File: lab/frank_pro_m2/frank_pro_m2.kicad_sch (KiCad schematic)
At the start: 12 parts, among them J1 UART, J2 PWR

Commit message: LAB WIP
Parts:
- removed JP1: Config Switches, FRANK:SOIC127P830X260-12N, symbol Switch:SW_DIP_x06
- added J3: PWR, FRANK:Pin Header (1x03), symbol Connector:Conn_01x03_Pin
- added JP1: Config Switches, FRANK:DS05127204BKSMTTR, symbol DS05-127-2-04BK-SMT-TR:DS05-127-2-04BK-SMT-TR
- added S1: MSK12C02, FRANK:SW_MSK12C02, symbol MSK12C02:MSK12C02
- added S3: RP BOOT, FRANK:TS-1234VW, symbol FRANK:SW_Push_1234VW
- added S4: RP Reset, FRANK:KMR_2, symbol KMR221G_LFS:KMR221G_LFS
- added S5: RP BOOT, FRANK:KMR_2, symbol KMR221G_LFS:KMR221G_LFS
- added S6: ESP Reset, FRANK:TS-1234VW, symbol FRANK:SW_Push_1234VW
- J1: footprint FRANK:Pin Header (1x03) -> FRANK:JST_SH_BM04B-SRSS-TB_1x04-1MP_P1.00mm_Vertical; symbol Connector:Conn_01x03_Pin -> Connector:Conn_01x04_Pin
- J2: value PWR -> DEBUG; footprint FRANK:Pin Header (1x03) -> FRANK:JST_SH_BM03B-SRSS-TB_1x03-1MP_P1.00mm_Vertical
- S2: renamed from S1; value Reset -> RP Reset; footprint FRANK:TACT-SIDE-4623 -> FRANK:TS-1234VW; symbol Switch:SW_Push -> FRANK:SW_Push_1234VW
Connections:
- net +3V3: now also J1.2 (Pin_2), J3.1 (Pin_1), JP1.4 (NO_2); no longer J2.1 (Pin_1)
- net AMP_L: now also JP1.7 (COM_4)
- net AUDIOSW: now also JP1.1 (COM_1)
- net ESP_RST: now also S6.1
- net GND: now also J1.1 (Pin_1), S2.3 (GND), J3.2 (Pin_2), JP1.6 (NO_3), S1.4_1 (GND), S1.4_2 (GND), S1.4_3 (GND), S1.4_4 (GND), S3.2, S3.3 (GND), S4.2, S4.4, S5.2, S5.4, S6.2, S6.3 (GND); no longer J1.3 (Pin_3)
- net MONO_R: now also JP1.8 (NO_4)
- net MSPUP3V3: now also JP1.3 (COM_2)
- net PGPIO0: now also J1.3 (Pin_3); no longer J1.1 (Pin_1)
- net PGPIO1: now also J1.4 (Pin_4); no longer J1.2 (Pin_2)
- net PRUN: now also S4.1, S4.3
- net PSWCLK: now also J2.1 (Pin_1)
- net PSWDIO: now also J2.3 (Pin_3)
- net SHND: now also JP1.5 (COM_3)
- net UM_SW: now also S1.3
- net VBUS: now also J3.3 (Pin_3), JP1.2 (NO_1), S1.2; no longer J2.3 (Pin_3)
- new net PBOOTSEL: S3.1, S5.1, S5.3
- no-connect marks 32 -> 33
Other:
- moved on the sheet: J2

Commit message: Board updates
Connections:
- net AMP_L: no longer JP1.7 (COM_4)
- new net MONO_L: JP1.7 (COM_4)
- no-connect marks 33 -> 32

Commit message: Rename footprints, 3D models to KiCad standard naming
lab/xt8086:
- Renamed 22 footprints (spaces/parens/IPNs -> KiCad style)
- Renamed 13 3D models, normalized all to .step
- Fixed FRANK: prefix -> xt8086: in symbol/schematic refs
- Fixed bare 3D model path without ${KIPRJMOD} prefix

lab/frank_pro_m2:
- Removed 11 unused footprints
- Renamed 32 footprints to KiCad standard naming
- Renamed 33 3D models, normalized all to .step
- Fixed wrong library prefixes (LIBS:, DC-005-5A-2.0:, MSK12C02:, etc.)
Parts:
- H1, H2, H3, H4: footprint FRANK:Mounting Hole (2.7mm) -> FRANK:MountingHole_2.7mm
- J1: footprint FRANK:JST_SH_BM04B-SRSS-TB_1x04-1MP_P1.00mm_Vertical -> FRANK:JST_SH_1x04_P1.00mm_Vertical
- J2: footprint FRANK:JST_SH_BM03B-SRSS-TB_1x03-1MP_P1.00mm_Vertical -> FRANK:JST_SH_1x03_P1.00mm_Vertical
- J3: footprint FRANK:Pin Header (1x03) -> FRANK:PinHeader_1x03_P2.54mm
- JP1: footprint FRANK:DS05127204BKSMTTR -> FRANK:DIPSwitch_4pos_DS05
- S1: footprint FRANK:SW_MSK12C02 -> FRANK:Switch_Slide_MSK12C02
- S2, S3, S6: footprint FRANK:TS-1234VW -> FRANK:Button_SMD_TS1234VW
- S4, S5: footprint FRANK:KMR_2 -> FRANK:Button_SMD_3x4x2mm
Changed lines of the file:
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@@
 			)
 		)
-		(property "Footprint" "FRANK:SW_MSK12C02"
+		(property "Footprint" "FRANK:Switch_Slide_MSK12C02"
 			(at 173.99 95.25 0)
 			(hide yes)
@@
 			)
 		)
-		(property "Footprint" "FRANK:DS05127204BKSMTTR"
+		(property "Footprint" "FRANK:DIPSwitch_4pos_DS05"
 			(at 207.01 125.4 0)
 			(hide yes)
@@
 			)
 		)
-		(property "Footprint" "FRANK:KMR_2"
+		(property "Footprint" "FRANK:Button_SMD_3x4x2mm"
 			(at 234.95 166.04 0)
 			(hide yes)
@@
 			)
 		)
-		(property "Footprint" "FRANK:JST_SH_BM03B-SRSS-TB_1x03-1MP_P1.00mm_Vertical"
+		(property "Footprint" "FRANK:JST_SH_1x03_P1.00mm_Vertical"
 			(at 226.06 93.98 0)
 			(hide yes)
@@
 			)
 		)
-		(property "Footprint" "FRANK:Pin Header (1x03)"
+		(property "Footprint" "FRANK:PinHeader_1x03_P2.54mm"
 			(at 252.73 93.98 0)
 			(hide yes)
@@
 			)
 		)
-		(property "Footprint" "FRANK:TS-1234VW"
+		(property "Footprint" "FRANK:Button_SMD_TS1234VW"
 			(at 184.15 53.34 0)
 			(hide yes)
@@
 			)
 		)
-		(property "Footprint" "FRANK:TS-1234VW"
+		(property "Footprint" "FRANK:Button_SMD_TS1234VW"
 			(at 184.15 68.58 0)
 			(hide yes)
@@
 			)
 		)
-		(property "Footprint" "FRANK:JST_SH_BM04B-SRSS-TB_1x04-1MP_P1.00mm_Vertical"
+		(property "Footprint" "FRANK:JST_SH_1x04_P1.00mm_Vertical"
 			(at 204.47 93.98 0)
 			(hide yes)
@@
 			)
 		)
-		(property "Footprint" "FRANK:Mounting Hole (2.7mm)"
+		(property "Footprint" "FRANK:MountingHole_2.7mm"
 			(at 160.02 187.96 0)
 			(hide yes)
@@
 			)
 		)
-		(property "Footprint" "FRANK:Mounting Hole (2.7mm)"
+		(property "Footprint" "FRANK:MountingHole_2.7mm"
 			(at 160.02 182.88 0)
 			(hide yes)
@@
 			)
 		)
-		(property "Footprint" "FRANK:Mounting Hole (2.7mm)"
+		(property "Footprint" "FRANK:MountingHole_2.7mm"
 			(at 160.02 193.04 0)
 			(hide yes)
@@
 			)
 		)
-		(property "Footprint" "FRANK:Mounting Hole (2.7mm)"
+		(property "Footprint" "FRANK:MountingHole_2.7mm"
 			(at 160.02 177.8 0)
 			(hide yes)
@@
 			)
 		)
-		(property "Footprint" "FRANK:TS-1234VW"
+		(property "Footprint" "FRANK:Button_SMD_TS1234VW"
 			(at 252.73 31.75 0)
 			(hide yes)
@@
 			)
 		)
-		(property "Footprint" "FRANK:KMR_2"
+		(property "Footprint" "FRANK:Button_SMD_3x4x2mm"
 			(at 234.95 150.8 0)
 			(hide yes)

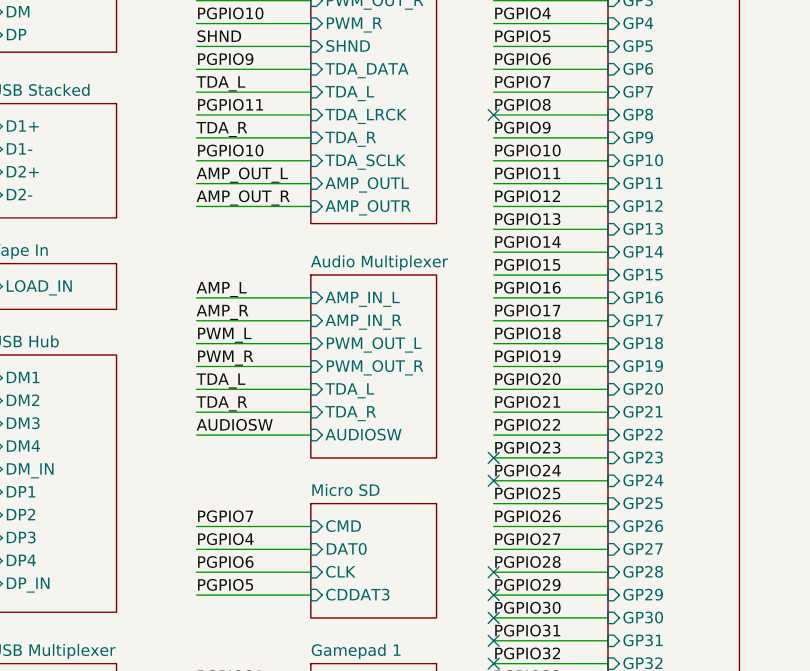
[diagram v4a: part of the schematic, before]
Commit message: Rename footprints and 3D models in lab/tinyfrank_m2p2
- Removed 2 unused footprints (ESP-01, SO-16)
- Renamed 18 footprints to KiCad standard naming
- Renamed 15 3D models, normalized all to .step
- Fixed wrong library prefixes (FRANK:, LIBS:, MSK12C02:, etc.)
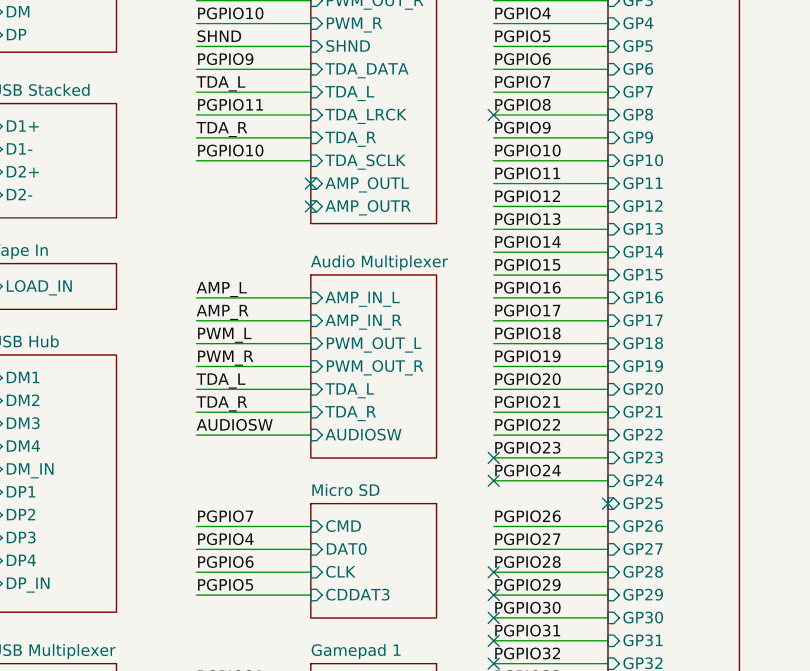
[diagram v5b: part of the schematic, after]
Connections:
- no-connect marks 32 -> 35
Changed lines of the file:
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@@
+	)
+	(no_connect
+		(at 134.62 96.52)
+	)
+	(no_connect
+		(at 101.6 60.96)
 	)
 	(no_connect
@@
 	)
 	(no_connect
+		(at 101.6 63.5)
+	)
+	(no_connect
 		(at 121.92 91.44)
 	)
@@
 	(wire
 		(pts
-			(xy 121.92 96.52) (xy 134.62 96.52)
-		)
-		(stroke
-			(width 0)
-			(type default)
-		)
-	)
-	(wire
-		(pts
 			(xy 88.9 45.72) (xy 101.6 45.72)
 		)
@@
 	(wire
 		(pts
-			(xy 88.9 60.96) (xy 101.6 60.96)
-		)
-		(stroke
-			(width 0)
-			(type default)
-		)
-	)
-	(wire
-		(pts
 			(xy 121.92 91.44) (xy 134.62 91.44)
 		)
@@
 		(pts
 			(xy 21.59 66.04) (xy 34.29 66.04)
-		)
-		(stroke
-			(width 0)
-			(type default)
-		)
-	)
-	(wire
-		(pts
-			(xy 88.9 63.5) (xy 101.6 63.5)
 		)
 		(stroke
@@
 		)
 	)
-	(label "PGPIO25"
-		(at 121.92 96.52 0)
-		(effects
-			(font
-				(size 1.27 1.27)
-			)
-			(justify left bottom)
-		)
-	)
-	(label "AMP_OUT_L"
-		(at 88.9 60.96 0)
-		(effects
-			(font
-				(size 1.27 1.27)
-			)
-			(justify left bottom)
-		)
-	)
 	(label "AUDIOSW"
 		(at 168.91 30.48 0)
@@
 		(effects
 			(font
-				(size 1.27 1.27)
-			)
-			(justify left bottom)
-		)
-	)
-	(label "AMP_OUT_R"
-		(at 88.9 63.5 0)
-		(effects
-			(font
